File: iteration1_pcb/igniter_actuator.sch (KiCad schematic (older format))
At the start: 21 parts

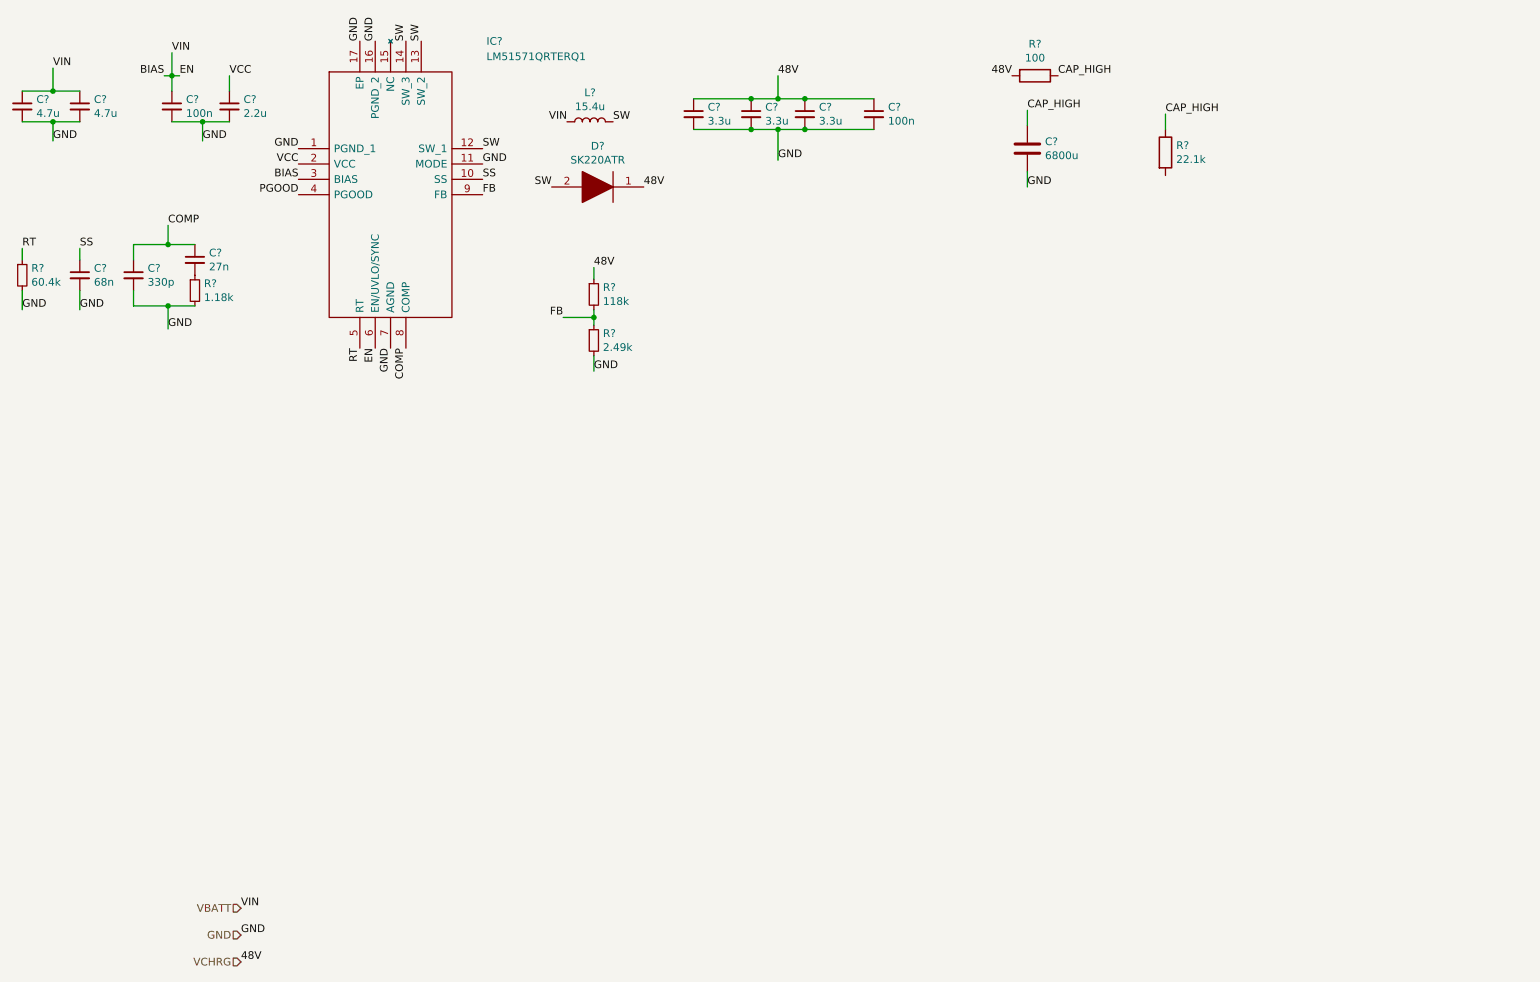
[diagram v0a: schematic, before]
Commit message: Cleaning individual part files and adding igniter actuator circuits
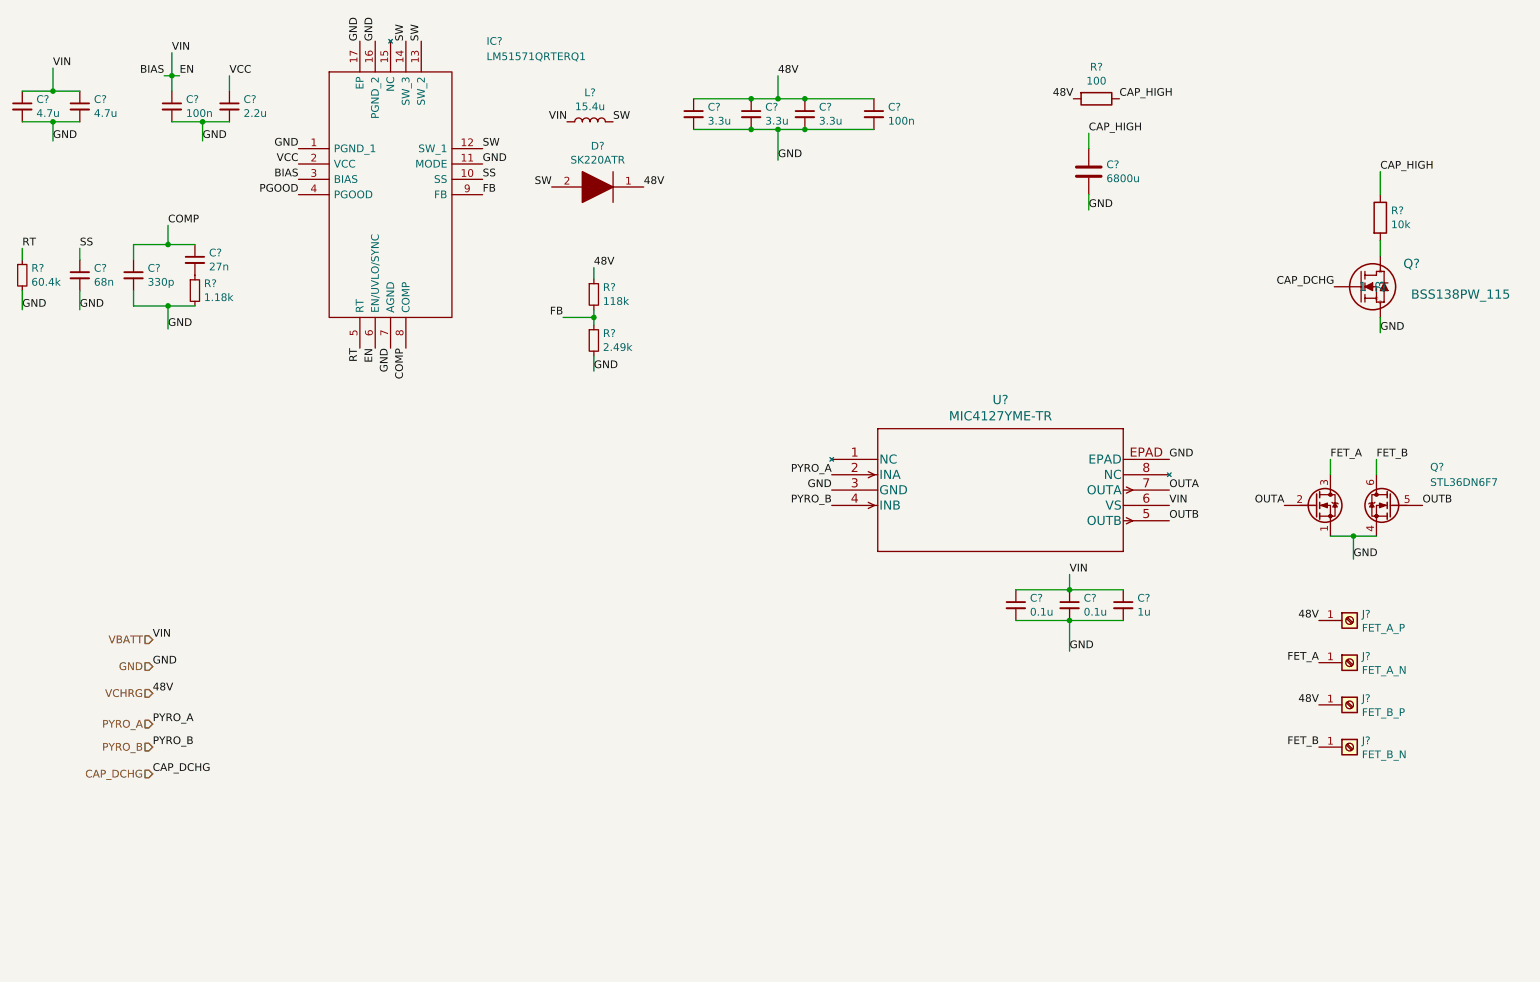
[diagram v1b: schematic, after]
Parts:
- removed R?: 22.1k, symbol Device:R
- added C? (x2): 0.1u, symbol Device:C_Small
- added C?: 1u, symbol Device:C_Small
- added J?: FET_A_P, symbol Connector:Screw_Terminal_01x01
- added J?: FET_A_N, symbol Connector:Screw_Terminal_01x01
- added J?: FET_B_P, symbol Connector:Screw_Terminal_01x01
- added J?: FET_B_N, symbol Connector:Screw_Terminal_01x01
- added Q?: STL36DN6F7, symbol symbols:STL36DN6F7
- added Q?: BSS138PW_115, SC-70_SOT323_NEX, symbol symbols:BSS138PW_115
- added R?: 10k, symbol Device:R
- added U?: MIC4127YME-TR, SOIC-8_ME_MCH, symbol symbols:MIC4127YME-TR
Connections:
- net CAP_HIGH: now also R?.1
- net GND: now also C?.2, C?.2, C?.2, Q?.1 (S), Q?.2, Q?.4 (S), U?.3 (GND), U?.EPAD
- net VBATT: now also C?.1, C?.1, C?.1, U?.6 (VS)
- net VCHRG: now also J?.1 (Pin_1), J?.1 (Pin_1)
- new net: Q?.3, R?.2
- new net CAP_DCHG: Q?.1
- new net FET_A: J?.1 (Pin_1), Q?.3 (D)
- new net FET_B: J?.1 (Pin_1), Q?.6 (D)
- new net OUTA: Q?.2 (G), U?.7 (OUTA)
- new net OUTB: Q?.5 (G), U?.5 (OUTB)
- new net PYRO_A: U?.2 (INA)
- new net PYRO_B: U?.4 (INB)
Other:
- moved on the sheet: C?, R?

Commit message: Adding schematic work
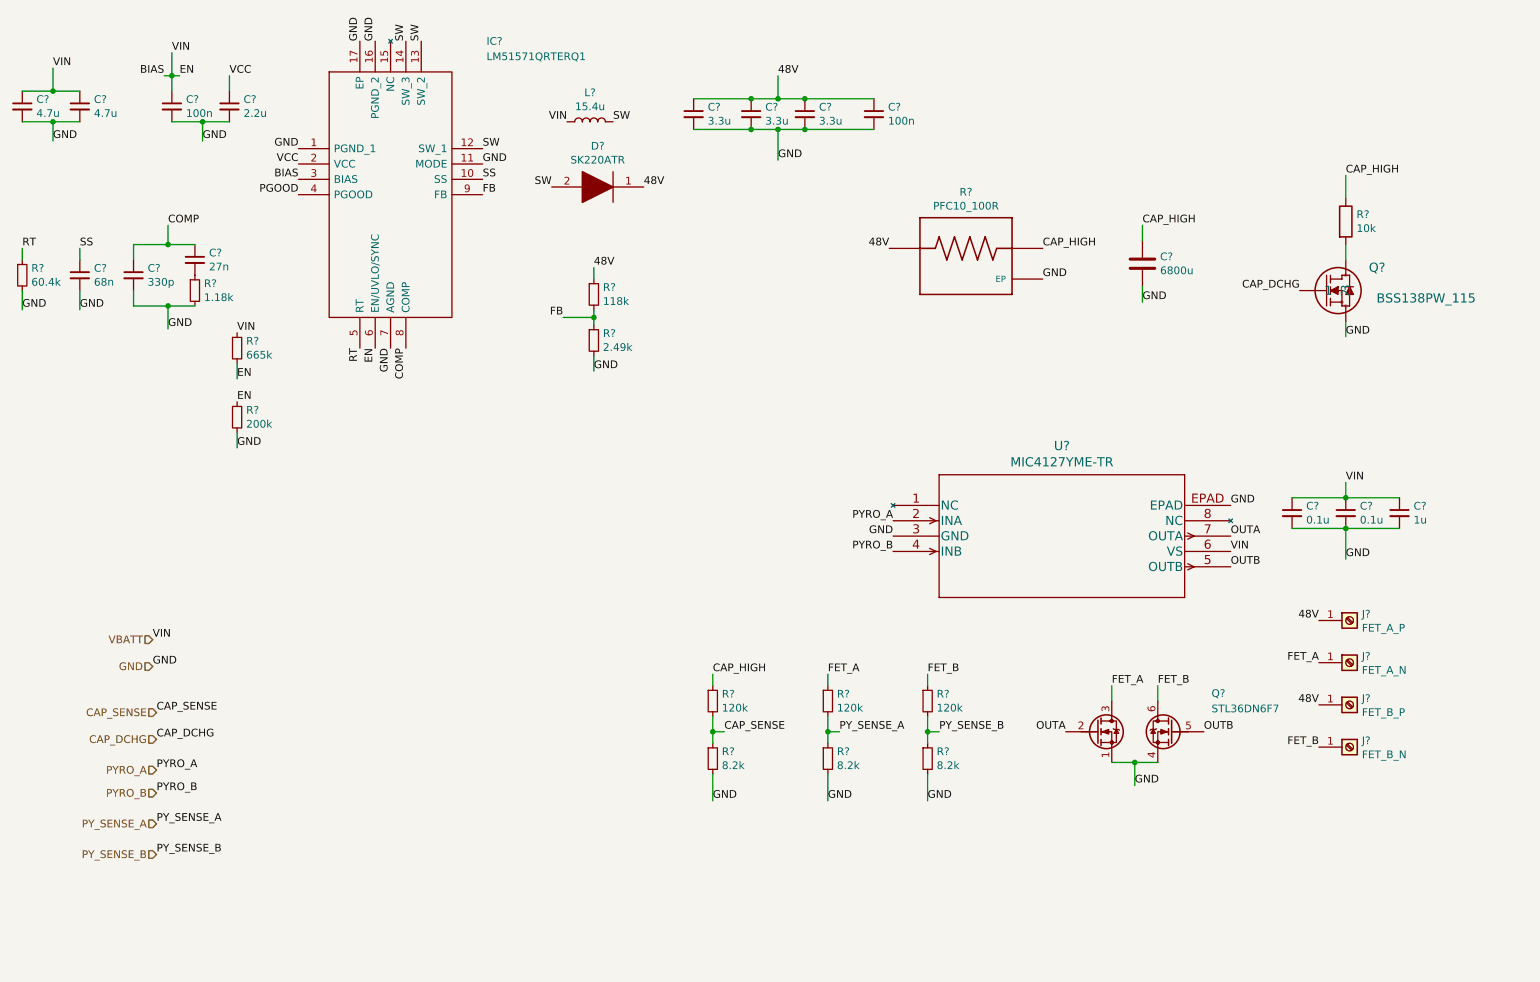
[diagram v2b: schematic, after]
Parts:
- removed R?: 100, symbol Device:R
- added R? (x3): 120k, symbol Device:R_Small
- added R? (x3): 8.2k, symbol Device:R_Small
- added R?: 665k, Resistor_SMD:R_0805_2012Metric_Pad1.20x1.40mm_HandSolder, symbol Device:R_Small
- added R?: 200k, Resistor_SMD:R_0603_1608Metric_Pad0.98x0.95mm_HandSolder, symbol Device:R_Small
- added R?: PFC10_100R, RES_PFC10, symbol symbols:PFC10
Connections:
- net CAP_HIGH: now also R?.1, R?.2
- net FET_A: now also R?.1
- net FET_B: now also R?.1
- net GND: now also R?.2, R?.2, R?.2, R?.2, R?.3 (EP)
- net VBATT: now also R?.1, R?.1, R?.2
- net VCHRG renamed 48V
- net 48V: now also R?.1
- new net CAP_SENSE: R?.1, R?.2
- new net PY_SENSE_A: R?.1, R?.2
- new net PY_SENSE_B: R?.1, R?.2
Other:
- moved on the sheet: C?, Q?, R?, U?
